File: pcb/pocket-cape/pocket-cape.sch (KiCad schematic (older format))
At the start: 26 parts, among them J1 Sync1, J10 Display, J11 USB1, J2 12..16V, J3 Sync2, J4 Sled, J5 Laser1, J6 PM1, J7 PM2, J8 Laser2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

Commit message: Wire up remaining connectors.
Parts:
- J9: value Inputs -> Switches
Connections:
- net labels added: BUTT_1, BUTT_2, BUTT_3
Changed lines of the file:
@@
 Text GLabel 9150 2250 2    40   Output ~ 0
 STEP_A1
-Text GLabel 4950 2850 2    40   Output ~ 0
+Text GLabel 1750 3350 0    40   Output ~ 0
 LASER1
-Text GLabel 4950 3550 2    40   Output ~ 0
+Text GLabel 1750 3550 0    40   Output ~ 0
 LASER2
 $Comp
@@
 Text GLabel 9150 3350 2    40   Input ~ 0
 Sync2
-Text GLabel 9150 3450 2    40   Input ~ 0
+Text GLabel 9150 3250 2    40   Input ~ 0
 Sync1
 $Comp
@@
 U 1 1 59D1AEC3
 P 9400 5450
-F 0 "J9" H 9550 5450 50  0000 C CNN
-F 1 "Inputs" V 9500 5300 50  0000 C CNN
+F 0 "J9" H 9400 5700 50  0000 C CNN
+F 1 "Switches" V 9500 5450 50  0000 C CNN
 F 2 "Connectors_JST:JST_PH_B4B-PH-K_04x2.00mm_Straight" H 9400 5450 50  0001 C CNN
 F 3 "" H 9400 5450 50  0001 C CNN
@@
 Wire Wire Line
 	8050 4500 7750 4500
+Text GLabel 9150 2850 2    40   Output ~ 0
+BUTT_3
+Text GLabel 6250 2750 0    40   Output ~ 0
+BUTT_1
+Text GLabel 6250 2850 0    40   Output ~ 0
+BUTT_2
+Text GLabel 9200 5500 0    40   Input ~ 0
+BUTT_1
+Text GLabel 9200 5400 0    40   Input ~ 0
+BUTT_2
+Text GLabel 9200 5300 0    40   Input ~ 0
+BUTT_3
 $EndSCHEMATC

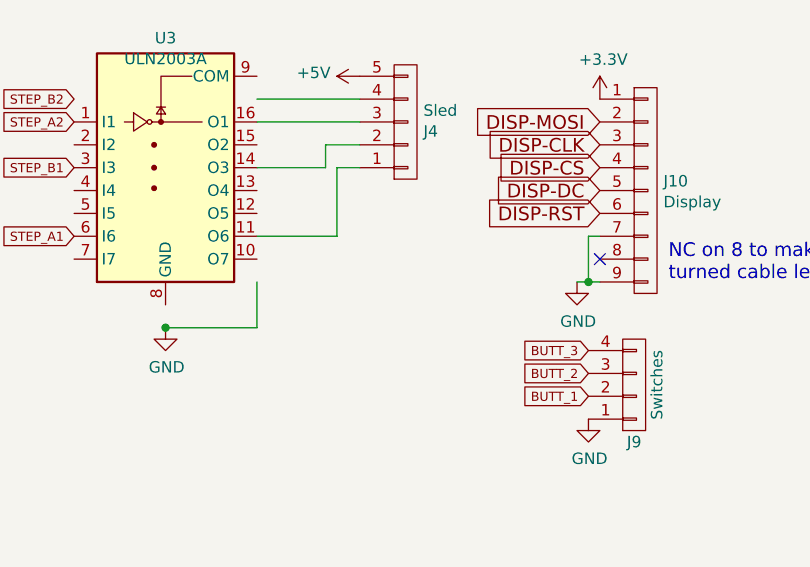
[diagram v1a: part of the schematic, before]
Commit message: Add a capacitor in the stepper driver vicinity.
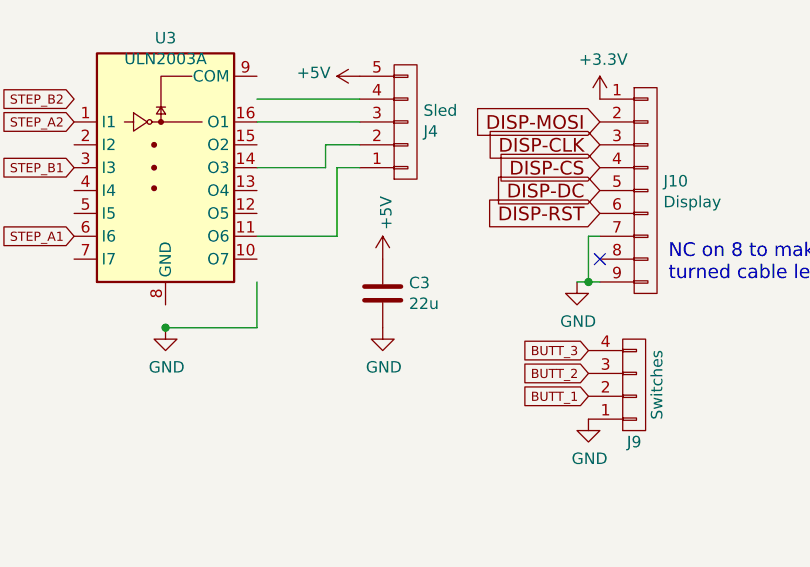
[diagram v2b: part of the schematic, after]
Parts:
- added C3: 22u, Capacitors_SMD:C_1206, symbol C
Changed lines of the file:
@@
 Text GLabel 9200 5300 0    40   Input ~ 0
 BUTT_3
+$Comp
+L C C3
+U 1 1 59D5BD4F
+P 8300 5050
+F 0 "C3" H 8415 5096 50  0000 L CNN
+F 1 "22u" H 8415 5005 50  0000 L CNN
+F 2 "Capacitors_SMD:C_1206" H 8338 4900 50  0001 C CNN
+F 3 "" H 8300 5050 50  0001 C CNN
+	1    8300 5050
+	1    0    0    -1
+$EndComp
+$Comp
+L GND #PWR030
+U 1 1 59D5BF45
+P 8300 5200
+F 0 "#PWR030" H 8300 4950 50  0001 C CNN
+F 1 "GND" H 8305 5027 50  0000 C CNN
+F 2 "" H 8300 5200 50  0001 C CNN
+F 3 "" H 8300 5200 50  0001 C CNN
+	1    8300 5200
+	1    0    0    -1
+$EndComp
+$Comp
+L +5V #PWR031
+U 1 1 59D5C014
+P 8300 4900
+F 0 "#PWR031" H 8300 4750 50  0001 C CNN
+F 1 "+5V" V 8315 5028 50  0000 L CNN
+F 2 "" H 8300 4900 50  0001 C CNN
+F 3 "" H 8300 4900 50  0001 C CNN
+	1    8300 4900
+	1    0    0    -1
+$EndComp
 $EndSCHEMATC

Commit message: Little tweaks (silk-screen; adding 100nF on 3.3V rail)
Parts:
- added C5: 100n, Capacitors_SMD:C_0603, symbol C
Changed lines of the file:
@@
+	1    0    0    -1
+$EndComp
+$Comp
+L GND #PWR032
+U 1 1 59D86721
+P 6250 5250
+F 0 "#PWR032" H 6250 5000 50  0001 C CNN
+F 1 "GND" H 6255 5077 50  0000 C CNN
+F 2 "" H 6250 5250 50  0001 C CNN
+F 3 "" H 6250 5250 50  0001 C CNN
+	1    6250 5250
+	1    0    0    -1
+$EndComp
+$Comp
+L C C5
+U 1 1 59D8672D
+P 6250 5100
+F 0 "C5" V 6300 5200 50  0000 C CNN
+F 1 "100n" V 6400 5100 50  0000 C CNN
+F 2 "Capacitors_SMD:C_0603" H 6288 4950 50  0001 C CNN
+F 3 "" H 6250 5100 50  0001 C CNN
+	1    6250 5100
+	-1   0    0    1
+$EndComp
+$Comp
+L +3.3V #PWR033
+U 1 1 59D8676E
+P 6250 4950
+F 0 "#PWR033" H 6250 4800 50  0001 C CNN
+F 1 "+3.3V" H 6265 5123 50  0000 C CNN
+F 2 "" H 6250 4950 50  0001 C CNN
+F 3 "" H 6250 4950 50  0001 C CNN
+	1    6250 4950
 	1    0    0    -1
 $EndComp

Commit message: Update values in Schematic; directly connect USB 5V with DC/DC 5V.
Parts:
- removed D1: D, Diodes_SMD:D_SOD-123, symbol D
- added D1: MBR230LSFT1G, Diodes_SMD:D_SOD-123, symbol D_Schottky
- J10: PartNo (none) -> SFv8R-4STBE1HLF
- R6: value R -> 6k2
- R7: value R -> 1k2
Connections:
- net labels removed: VCC
- no-connect marks 1 -> 41
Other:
- note added: "NC on 8 to make accidentally\nturned cable less dangerous.\n(pin 9 = connector shield)"
- note removed: "NC on 8 to make accidentally\nturned cable less dangerous."
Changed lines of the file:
@@
-EESchema Schematic File Version 2
+EESchema Schematic File Version 3
 LIBS:power
 LIBS:device
@@
 L GND #GND013
 U 1 1 599213A3
-P 1750 2650
-F 0 "#GND013" H 1651 2550 70  0001 L BNN
-F 1 "GND" V 1800 2300 70  0000 L BNN
-F 2 "" H 1750 2650 60  0001 C CNN
-F 3 "" H 1750 2650 60  0001 C CNN
-	1    1750 2650
-	0    1    1    0
+P 1550 2650
+F 0 "#GND013" H 1451 2550 70  0001 L BNN
+F 1 "GND" V 1600 2300 70  0000 L BNN
+F 2 "" H 1550 2650 60  0001 C CNN
+F 3 "" H 1550 2650 60  0001 C CNN
+	1    1550 2650
+	1    0    0    -1
 $EndComp
 $Comp
@@
 Text Label 6350 2550 0    65   ~ 0
 SYS_5V
-Text Label 1850 2250 0    65   ~ 0
-USB_DC
 Text Label 6350 3050 0    65   ~ 0
 VDD_3V3B
@@
 Text GLabel 3200 2250 0    10   UnSpc ~ 0
 USB_DC
-Text GLabel 1650 2250 2    10   UnSpc ~ 0
-USB_DC
-Text GLabel 5050 2550 0    10   UnSpc ~ 0
-VDD_3V3B
 Text GLabel 5700 3050 2    10   UnSpc ~ 0
 VDD_3V3B
@@
 $EndComp
 $Comp
-L D D1
-U 1 1 59CBB44D
-P 3000 4850
-F 0 "D1" V 2954 4929 50  0000 L CNN
-F 1 "D" V 3045 4929 50  0000 L CNN
-F 2 "Diodes_SMD:D_SOD-123" H 3000 4850 50  0001 C CNN
-F 3 "" H 3000 4850 50  0001 C CNN
-	1    3000 4850
-	0    1    1    0
-$EndComp
-$Comp
 L C C4
 U 1 1 59CBB589
@@
 P 3500 4550
 F 0 "R6" H 3350 4600 50  0000 L CNN
-F 1 "R" V 3500 4500 50  0000 L CNN
+F 1 "6k2" V 3500 4500 50  0000 L CNN
 F 2 "Resistors_SMD:R_0603" H 3570 4459 50  0001 L CNN
 F 3 "" H 3500 4550 50  0001 C CNN
@@
 P 3500 4850
 F 0 "R7" H 3350 4900 50  0000 L CNN
-F 1 "R" V 3500 4800 50  0000 L CNN
+F 1 "1k2" V 3500 4800 50  0000 L CNN
 F 2 "Resistors_SMD:R_0603" H 3570 4759 50  0001 L CNN
 F 3 "" H 3500 4850 50  0001 C CNN
@@
 P 3700 5450
 F 0 "J7" H 3778 5491 50  0000 L CNN
-F 1 "PM2" H 3600 5100 50  0000 L CNN
+F 1 "PM2" H 3650 5150 50  0000 L CNN
 F 2 "Pin_Headers:Pin_Header_Straight_1x05_Pitch2.54mm" H 3700 5450 50  0001 C CNN
 F 3 "" H 3700 5450 50  0001 C CNN
@@
 P 2900 5450
 F 0 "J6" H 2978 5491 50  0000 L CNN
-F 1 "PM1" H 3000 5150 50  0000 L CNN
+F 1 "PM1" H 2850 5150 50  0000 L CNN
 F 2 "Pin_Headers:Pin_Header_Straight_1x05_Pitch2.54mm" H 2900 5450 50  0001 C CNN
 F 3 "" H 2900 5450 50  0001 C CNN
@@
 F 3 "" H 4850 4200 50  0001 C CNN
 	1    4850 4200
-	1    0    0    -1
-$EndComp
-$Comp
-L VCC #PWR09
-U 1 1 59D194BA
-P 5700 4250
-F 0 "#PWR09" H 5700 4100 50  0001 C CNN
-F 1 "VCC" H 5717 4423 50  0000 C CNN
-F 2 "" H 5700 4250 50  0001 C CNN
-F 3 "" H 5700 4250 50  0001 C CNN
-	1    5700 4250
-	1    0    0    -1
-$EndComp
-$Comp
-L +3.3V #PWR011
-U 1 1 59D196D2
-P 5950 4250
-F 0 "#PWR011" H 5950 4100 50  0001 C CNN
-F 1 "+3.3V" H 5965 4423 50  0000 C CNN
-F 2 "" H 5950 4250 50  0001 C CNN
-F 3 "" H 5950 4250 50  0001 C CNN
-	1    5950 4250
 	1    0    0    -1
 $EndComp
@@
 F 2 "ldgraphy.pretty:FlatFlexConn-08" H 9450 4600 50  0001 C CNN
 F 3 "" H 9450 4600 50  0001 C CNN
+F 4 "SFv8R-4STBE1HLF" H 9450 4600 60  0001 C CNN "PartNo"
 	1    9450 4600
 	1    0    0    -1
 $EndComp
 NoConn ~ 9250 4900
-Text Notes 9550 5000 0    60   ~ 0
-NC on 8 to make accidentally\nturned cable less dangerous.
+Text Notes 9550 5150 0    60   ~ 0
+NC on 8 to make accidentally\nturned cable less dangerous.\n(pin 9 = connector shield)
 $Comp
 L CONN_01X05 J11
@@
 	6250 3650 7450 3650
 Wire Wire Line
-	950  2550 3250 2550
-Wire Wire Line
 	950  2450 3250 2450
 Wire Wire Line
@@
 	3250 2050 1750 2050
 Wire Wire Line
-	1300 2150 3250 2150
-Wire Wire Line
 	9150 3650 7950 3650
 Wire Wire Line
@@
 	9150 2650 7950 2650
 Wire Wire Line
-	1750 2650 3250 2650
+	1550 2650 3250 2650
 Wire Wire Line
 	4950 2650 3750 2650
@@
 Wire Wire Line
 	6150 2550 7450 2550
-Wire Wire Line
-	950  2250 3250 2250
 Wire Wire Line
 	5700 3050 7450 3050
@@
 Connection ~ 5700 3050
 Wire Wire Line
-	5700 4250 5950 4250
-Wire Wire Line
-	9250 5000 9150 5000
+	9150 5000 9250 5000
 Wire Wire Line
 	9250 4800 9200 4800
@@
 Wire Wire Line
 	1300 2250 1300 2150
-Connection ~ 1300 2250
-Connection ~ 1650 2250
 Wire Wire Line
 	1750 2650 1750 2550
-Connection ~ 1750 2550
 $Comp
 L GND #GND01
@@
 	1    0    0    -1
 $EndComp
+Wire Wire Line
+	1300 2150 3250 2150
+Wire Wire Line
+	950  2250 1300 2250
+$Comp
+L +5V #PWR09
+U 1 1 59E06EFD
+P 1000 2250
+F 0 "#PWR09" H 1000 2100 50  0001 C CNN
+F 1 "+5V" H 1015 2423 50  0000 C CNN
+F 2 "" H 1000 2250 50  0001 C CNN
+F 3 "" H 1000 2250 50  0001 C CNN
+	1    1000 2250
+	1    0    0    -1
+$EndComp
+Connection ~ 1000 2250
+Wire Wire Line
+	950  2550 950  2650
+Wire Wire Line
+	1750 2550 3250 2550
+Connection ~ 1750 2650
+NoConn ~ 9150 2450
+NoConn ~ 9150 2550
+NoConn ~ 9150 2650
+NoConn ~ 9150 3150
+NoConn ~ 9150 3450
+NoConn ~ 9150 3550
+NoConn ~ 9150 3650
+NoConn ~ 6250 3250
+NoConn ~ 6250 1950
+NoConn ~ 6250 2050
+NoConn ~ 6250 2150
+NoConn ~ 6250 2250
+NoConn ~ 6250 2350
+NoConn ~ 6250 2450
+NoConn ~ 1750 2750
+NoConn ~ 1750 2850
+NoConn ~ 1750 2950
+NoConn ~ 1750 3050
+NoConn ~ 1750 3150
+NoConn ~ 1750 3250
+NoConn ~ 1750 3450
+NoConn ~ 1750 3650
+NoConn ~ 4950 3650
+NoConn ~ 4950 3550
+NoConn ~ 4950 3450
+NoConn ~ 4950 3350
+NoConn ~ 4950 3250
+NoConn ~ 4950 3150
+NoConn ~ 4950 2850
+NoConn ~ 4950 2750
+NoConn ~ 4950 2450
+NoConn ~ 4950 2350
+NoConn ~ 4950 2250
+NoConn ~ 4950 2150
+NoConn ~ 4950 2050
+NoConn ~ 4950 1950
+NoConn ~ 2700 5350
+NoConn ~ 3500 5350
+NoConn ~ 1750 2050
+NoConn ~ 9150 1950
+$Comp
+L D_Schottky D1
+U 1 1 59F5AC61
+P 3000 4850
+F 0 "D1" V 2954 4929 50  0000 L CNN
+F 1 "MBR230LSFT1G" V 3200 4350 50  0000 L CNN
+F 2 "Diodes_SMD:D_SOD-123" H 3000 4850 50  0001 C CNN
+F 3 "" H 3000 4850 50  0001 C CNN
+	1    3000 4850
+	0    1    1    0
+$EndComp
 $EndSCHEMATC

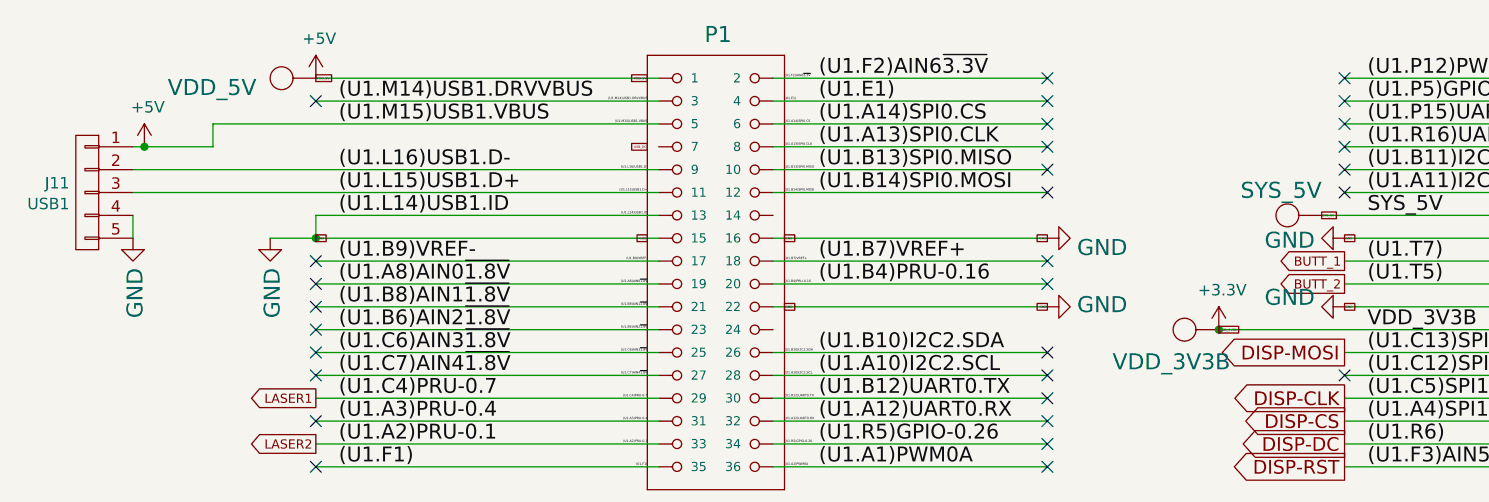
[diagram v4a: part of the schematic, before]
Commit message: Connect USB output to SYS 5V
o SYS 5V has a cleaner switch-on transition than the raw DC/DC out.
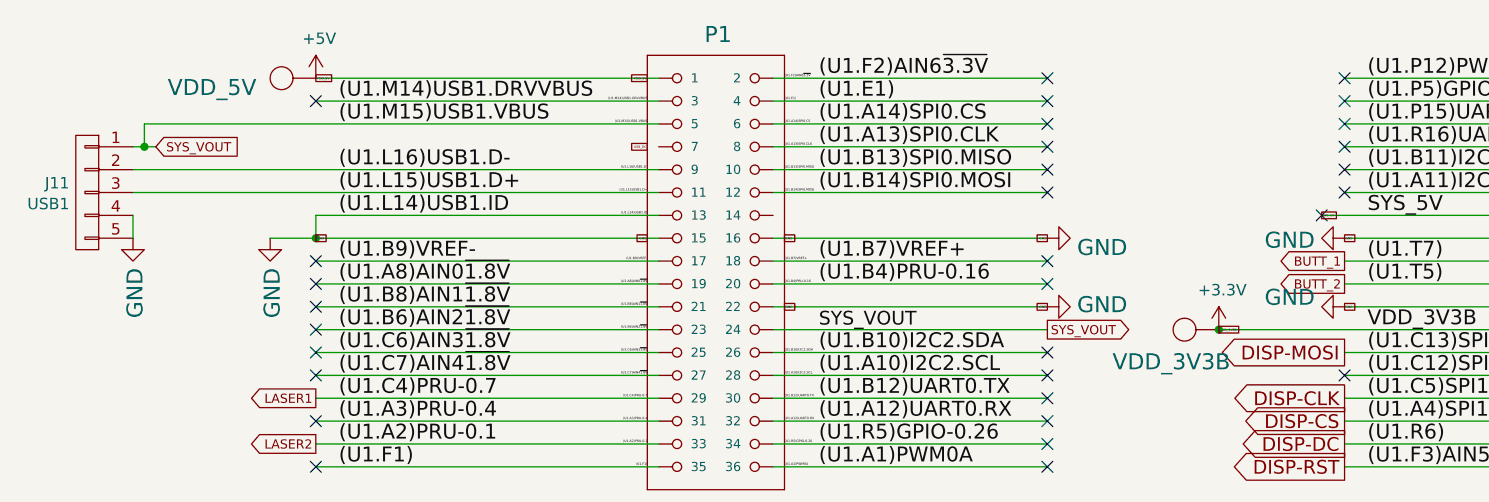
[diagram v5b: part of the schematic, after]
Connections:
- net +5V: no longer J11.1 (P1), P1.5
- net SYS_VOUT: now reaches P1.24
- net SYS_VOUT: now also J11.1 (P1), P1.5
- no-connect marks 41 -> 42
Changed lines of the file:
@@
-$EndComp
-$Comp
-L SYS_5V #SUPPLY05
-U 1 1 59922B13
-P 6050 2550
-F 0 "#SUPPLY05" H 6050 2710 70  0001 L BNN
-F 1 "SYS_5V" V 6200 2450 70  0000 L BNN
-F 2 "" H 6050 2550 60  0001 C CNN
-F 3 "" H 6050 2550 60  0001 C CNN
-	1    6050 2550
-	0    -1   -1   0
 $EndComp
 $Comp
@@
 Connection ~ 9200 5000
 Wire Wire Line
-	1300 2250 1300 2150
-Wire Wire Line
 	1750 2650 1750 2550
 $Comp
@@
 $EndComp
 Wire Wire Line
-	1300 2150 3250 2150
-Wire Wire Line
-	950  2250 1300 2250
-$Comp
-L +5V #PWR09
-U 1 1 59E06EFD
-P 1000 2250
-F 0 "#PWR09" H 1000 2100 50  0001 C CNN
-F 1 "+5V" H 1015 2423 50  0000 C CNN
-F 2 "" H 1000 2250 50  0001 C CNN
-F 3 "" H 1000 2250 50  0001 C CNN
-	1    1000 2250
-	1    0    0    -1
-$EndComp
-Connection ~ 1000 2250
+	1000 2150 3250 2150
 Wire Wire Line
 	950  2550 950  2650
@@
 	0    1    1    0
 $EndComp
+Wire Wire Line
+	4950 3050 3750 3050
+Text Label 3950 3050 0    60   ~ 0
+SYS_VOUT
+Text GLabel 4950 3050 2    40   Output ~ 0
+SYS_VOUT
+Text GLabel 1050 2250 2    40   Input ~ 0
+SYS_VOUT
+Wire Wire Line
+	950  2250 1050 2250
+Wire Wire Line
+	1000 2150 1000 2250
+Connection ~ 1000 2250
+NoConn ~ 6150 2550
 $EndSCHEMATC

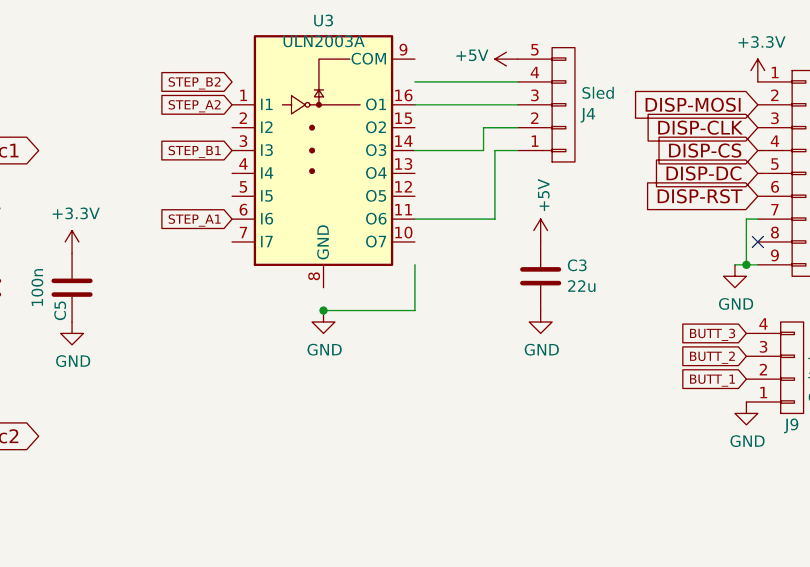
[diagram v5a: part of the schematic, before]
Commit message: Connect flyback diodes to +5V.
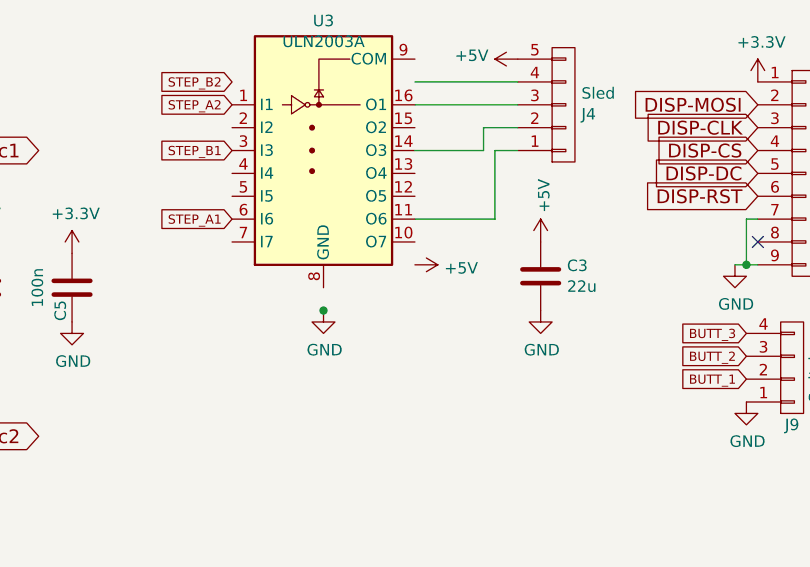
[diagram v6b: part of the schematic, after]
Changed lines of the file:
@@
 LIBS:power
 LIBS:device
-LIBS:transistors
-LIBS:conn
-LIBS:linear
-LIBS:regul
-LIBS:74xx
-LIBS:cmos4000
-LIBS:adc-dac
-LIBS:memory
-LIBS:xilinx
-LIBS:microcontrollers
-LIBS:dsp
-LIBS:microchip
-LIBS:analog_switches
-LIBS:motorola
-LIBS:texas
-LIBS:intel
-LIBS:audio
-LIBS:interface
-LIBS:digital-audio
-LIBS:philips
-LIBS:display
-LIBS:cypress
-LIBS:siliconi
-LIBS:opto
-LIBS:atmel
-LIBS:contrib
-LIBS:valves
-LIBS:ldgraphy
 LIBS:pocket-cape-cache
 EELAYER 26 0
@@
 Wire Wire Line
 	7750 4300 8200 4300
-Wire Wire Line
-	7350 5200 7750 5200
-Wire Wire Line
-	7750 5200 7750 5000
 Connection ~ 7350 5200
 Wire Wire Line
@@
 Connection ~ 1000 2250
 NoConn ~ 6150 2550
+$Comp
+L +5V #PWR?
+U 1 1 59F5543E
+P 7750 5000
+F 0 "#PWR?" H 7750 4850 50  0001 C CNN
+F 1 "+5V" V 7765 5128 50  0000 L CNN
+F 2 "" H 7750 5000 50  0001 C CNN
+F 3 "" H 7750 5000 50  0001 C CNN
+	1    7750 5000
+	0    1    1    0
+$EndComp
 $EndSCHEMATC

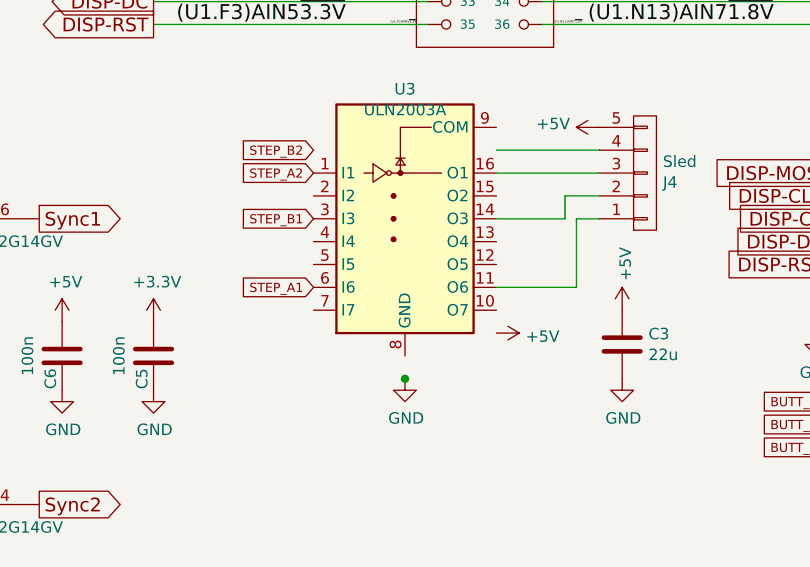
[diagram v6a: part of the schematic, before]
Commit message: More cooling for ULN2003
o Connect unused pins to a GND copper plane for slightly better
  heat distribution (in any case, we are well within ratings
  of the chip; the sum of all currents is never more than 500mA).
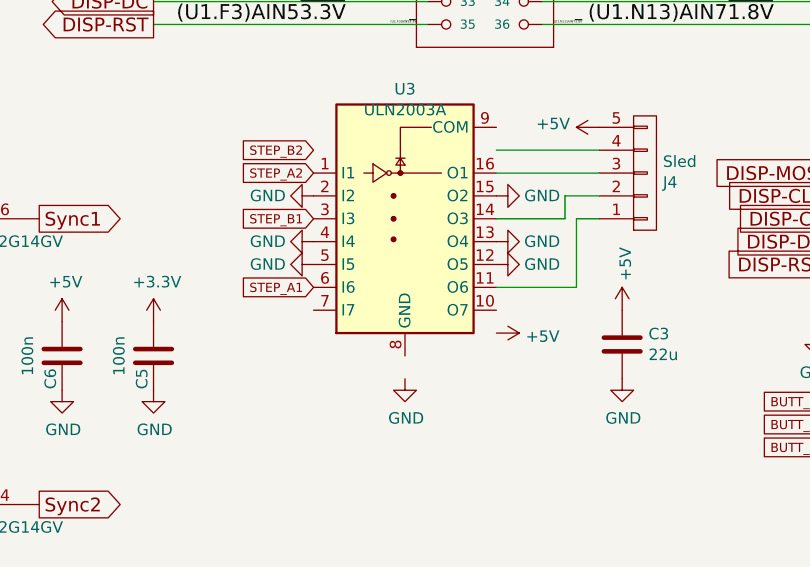
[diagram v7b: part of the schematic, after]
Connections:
- net GND: now also U3.12 (O5), U3.13 (O4), U3.15 (O2), U3.2 (I2), U3.4 (I4), U3.5 (I5)
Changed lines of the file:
@@
 Wire Wire Line
 	7750 4300 8200 4300
-Connection ~ 7350 5200
 Wire Wire Line
 	2700 5250 3500 5250
@@
 	0    1    1    0
 $EndComp
+$Comp
+L GND #PWR?
+U 1 1 59F56D9F
+P 6950 4400
+F 0 "#PWR?" H 6950 4150 50  0001 C CNN
+F 1 "GND" V 6950 4200 50  0000 C CNN
+F 2 "" H 6950 4400 50  0001 C CNN
+F 3 "" H 6950 4400 50  0001 C CNN
+	1    6950 4400
+	0    1    1    0
+$EndComp
+$Comp
+L GND #PWR?
+U 1 1 59F56E7F
+P 6950 4600
+F 0 "#PWR?" H 6950 4350 50  0001 C CNN
+F 1 "GND" V 6950 4400 50  0000 C CNN
+F 2 "" H 6950 4600 50  0001 C CNN
+F 3 "" H 6950 4600 50  0001 C CNN
+	1    6950 4600
+	0    1    1    0
+$EndComp
+$Comp
+L GND #PWR?
+U 1 1 59F56EC4
+P 6950 4700
+F 0 "#PWR?" H 6950 4450 50  0001 C CNN
+F 1 "GND" V 6950 4500 50  0000 C CNN
+F 2 "" H 6950 4700 50  0001 C CNN
+F 3 "" H 6950 4700 50  0001 C CNN
+	1    6950 4700
+	0    1    1    0
+$EndComp
+$Comp
+L GND #PWR?
+U 1 1 59F56F09
+P 7750 4700
+F 0 "#PWR?" H 7750 4450 50  0001 C CNN
+F 1 "GND" V 7750 4500 50  0000 C CNN
+F 2 "" H 7750 4700 50  0001 C CNN
+F 3 "" H 7750 4700 50  0001 C CNN
+	1    7750 4700
+	0    -1   -1   0
+$EndComp
+$Comp
+L GND #PWR?
+U 1 1 59F56F88
+P 7750 4600
+F 0 "#PWR?" H 7750 4350 50  0001 C CNN
+F 1 "GND" V 7750 4400 50  0000 C CNN
+F 2 "" H 7750 4600 50  0001 C CNN
+F 3 "" H 7750 4600 50  0001 C CNN
+	1    7750 4600
+	0    -1   -1   0
+$EndComp
+$Comp
+L GND #PWR?
+U 1 1 59F56FCD
+P 7750 4400
+F 0 "#PWR?" H 7750 4150 50  0001 C CNN
+F 1 "GND" V 7750 4200 50  0000 C CNN
+F 2 "" H 7750 4400 50  0001 C CNN
+F 3 "" H 7750 4400 50  0001 C CNN
+	1    7750 4400
+	0    -1   -1   0
+$EndComp
 $EndSCHEMATC
